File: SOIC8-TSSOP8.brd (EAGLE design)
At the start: 17.4 x 12.7 mm, 7 parts

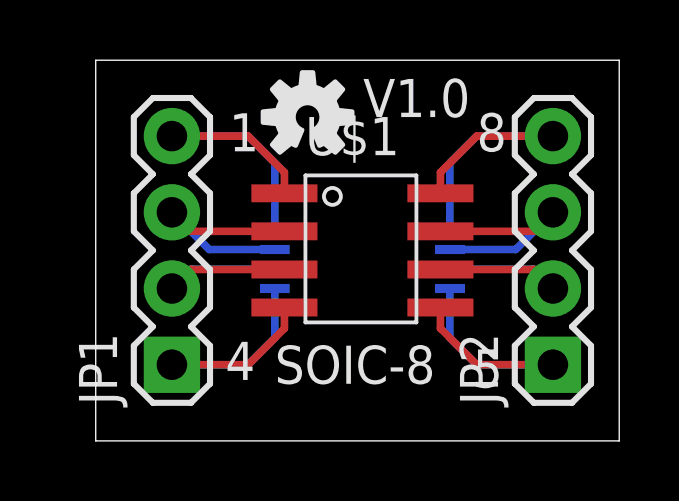
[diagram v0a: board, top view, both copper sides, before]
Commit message: Silk and board revision
Worked several silk screen issues and narrowed some boards.
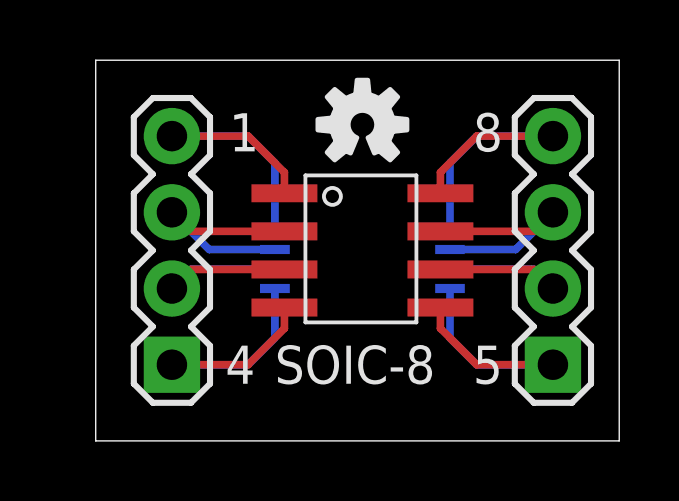
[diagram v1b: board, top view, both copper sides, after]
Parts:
- moved U$3 1.85 mm to (8.89, 25.8)
- moved U$4 0.38 mm to (8.89, 25.8)
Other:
- board text added: "2"
- board text added: "3"
- board text added: "6"
- board text added: "7"
- board text removed: "V1.0"
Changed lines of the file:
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@@
 <?xml version="1.0" encoding="utf-8"?>
 <!DOCTYPE eagle SYSTEM "eagle.dtd">
-<eagle version="7.2.0">
+<eagle version="7.3.0">
 <drawing>
 <settings>
@@
 <layer number="23" name="tOrigins" color="15" fill="1" visible="yes" active="yes"/>
 <layer number="24" name="bOrigins" color="15" fill="1" visible="yes" active="yes"/>
-<layer number="25" name="tNames" color="7" fill="1" visible="yes" active="yes"/>
-<layer number="26" name="bNames" color="7" fill="1" visible="yes" active="yes"/>
-<layer number="27" name="tValues" color="7" fill="1" visible="yes" active="yes"/>
-<layer number="28" name="bValues" color="7" fill="1" visible="yes" active="yes"/>
+<layer number="25" name="tNames" color="7" fill="1" visible="no" active="yes"/>
+<layer number="26" name="bNames" color="7" fill="1" visible="no" active="yes"/>
+<layer number="27" name="tValues" color="7" fill="1" visible="no" active="yes"/>
+<layer number="28" name="bValues" color="7" fill="1" visible="no" active="yes"/>
 <layer number="29" name="tStop" color="7" fill="3" visible="no" active="yes"/>
 <layer number="30" name="bStop" color="7" fill="6" visible="no" active="yes"/>
@@
 <layer number="50" name="dxf" color="7" fill="1" visible="no" active="no"/>
 <layer number="51" name="tDocu" color="6" fill="1" visible="yes" active="yes"/>
-<layer number="52" name="bDocu" color="7" fill="1" visible="yes" active="yes"/>
+<layer number="52" name="bDocu" color="7" fill="1" visible="no" active="yes"/>
 <layer number="53" name="tGND_GNDA" color="7" fill="9" visible="no" active="no"/>
 <layer number="54" name="bGND_GNDA" color="1" fill="9" visible="no" active="no"/>
@@
 <text x="12.827" y="17.78" size="1.27" layer="22" rot="MR0">TSSOP-8</text>
 <text x="5.969" y="17.145" size="1.27" layer="21">SOIC-8</text>
-<text x="8.9154" y="26.035" size="1.27" layer="21">V1.0</text>
 <text x="4.445" y="24.892" size="1.27" layer="21">1</text>
-<text x="4.318" y="17.272" size="1.27" layer="21">4</text>
-<text x="12.573" y="17.018" size="1.27" layer="21">5</text>
-<text x="12.7" y="24.892" size="1.27" layer="21">8</text>
-<text x="13.843" y="24.892" size="1.27" layer="22" rot="MR0">1</text>
-<text x="13.97" y="17.399" size="1.27" layer="22" rot="MR0">4</text>
-<text x="4.953" y="17.145" size="1.27" layer="22" rot="MR0">5</text>
-<text x="4.699" y="24.765" size="1.27" layer="22" rot="MR0">8</text>
+<text x="4.318" y="17.145" size="1.27" layer="21">4</text>
+<text x="12.573" y="17.145" size="1.27" layer="21">5</text>
+<text x="12.573" y="24.892" size="1.27" layer="21">8</text>
+<text x="13.843" y="24.765" size="1.27" layer="22" rot="MR0">1</text>
+<text x="13.97" y="17.272" size="1.27" layer="22" rot="MR0">4</text>
+<text x="4.826" y="17.018" size="1.27" layer="22" rot="MR0">5</text>
+<text x="4.826" y="24.765" size="1.27" layer="22" rot="MR0">8</text>
 <text x="16.764" y="-2.794" size="1.778" layer="51">Kevin Neubauer</text>
+<text x="13.843" y="22.225" size="1.27" layer="22" rot="MR0">2</text>
+<text x="13.843" y="19.685" size="1.27" layer="22" rot="MR0">3</text>
+<text x="4.826" y="22.225" size="1.27" layer="22" rot="MR0">7</text>
+<text x="4.826" y="19.685" size="1.27" layer="22" rot="MR0">6</text>
 </plain>
 <attributes>
@@
 <elements>
 <element name="FRAME1" library="SparkFun-Aesthetics" package="CREATIVE_COMMONS" value="FRAME-LETTER" x="-9.652" y="-2.7432"/>
-<element name="U$3" library="SparkFun-Aesthetics" package="OSHW-LOGO-S" value="" x="7.0612" y="26.035"/>
-<element name="U$4" library="SparkFun-Aesthetics" package="OSHW-LOGO-S" value="" x="8.8392" y="25.4" rot="MR0"/>
-<element name="U$1" library="Kevin-GenericICFootprints" package="SOIC-8" value="SOIC-8" x="8.89" y="21.59" smashed="yes" rot="R270">
-<attribute name="NAME" x="6.985" y="24.765" size="1.27" layer="25" font="vector" ratio="10"/>
-<attribute name="VALUE" x="6.985" y="17.145" size="1.27" layer="27" font="vector" ratio="10"/>
+<element name="U$3" library="SparkFun-Aesthetics" package="OSHW-LOGO-S" value="" x="8.89" y="25.781"/>
+<element name="U$4" library="SparkFun-Aesthetics" package="OSHW-LOGO-S" value="" x="8.89" y="25.781" rot="MR0"/>
+<element name="U$1" library="Kevin-GenericICFootprints" package="SOIC-8" value="SOIC-8" x="8.89" y="21.59" smashed="yes" rot="R270"/>
+<element name="U$2" library="Kevin-GenericICFootprints" package="TSSOP8" value="TSSOP-8" x="8.89" y="21.59" smashed="yes" rot="MR270"/>
+<element name="JP1" library="SparkFun-Connectors" package="1X04" value="" x="2.54" y="17.78" smashed="yes" rot="R90">
+<attribute name="VALUE" x="5.715" y="16.51" size="1.27" layer="27" rot="R90"/>
 </element>
-<element name="U$2" library="Kevin-GenericICFootprints" package="TSSOP8" value="TSSOP-8" x="8.89" y="21.59" smashed="yes" rot="MR270"/>
-<element name="JP1" library="SparkFun-Connectors" package="1X04" value="" x="2.54" y="17.78" rot="R90"/>
-<element name="JP2" library="SparkFun-Connectors" package="1X04" value="" x="15.24" y="17.78" rot="R90"/>
+<element name="JP2" library="SparkFun-Connectors" package="1X04" value="" x="15.24" y="17.78" smashed="yes" rot="R90">
+<attribute name="VALUE" x="18.415" y="16.51" size="1.27" layer="27" rot="R90"/>
+</element>
 </elements>
 <signals>
